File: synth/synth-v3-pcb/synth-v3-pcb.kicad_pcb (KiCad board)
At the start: 2 copper layers, 213.5 x 130 mm, 78 parts, among them J1 Keyboard, J2 15mm Touch, J3 15mm Touch, J4 3.5mm Jack, U1 LM324N, U2 LM324N, U3 LM324N, U4 Pi Pico, U5 TC1044S, U6 NJM4580D

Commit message: Released Synth V3.0
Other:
- board text added: "DO NOT PLACE COMPONENTS ON THIS SIDE OF THE BOARD"
- board text added: "LIVEWIRES SYNTH SOLDER SIDE"

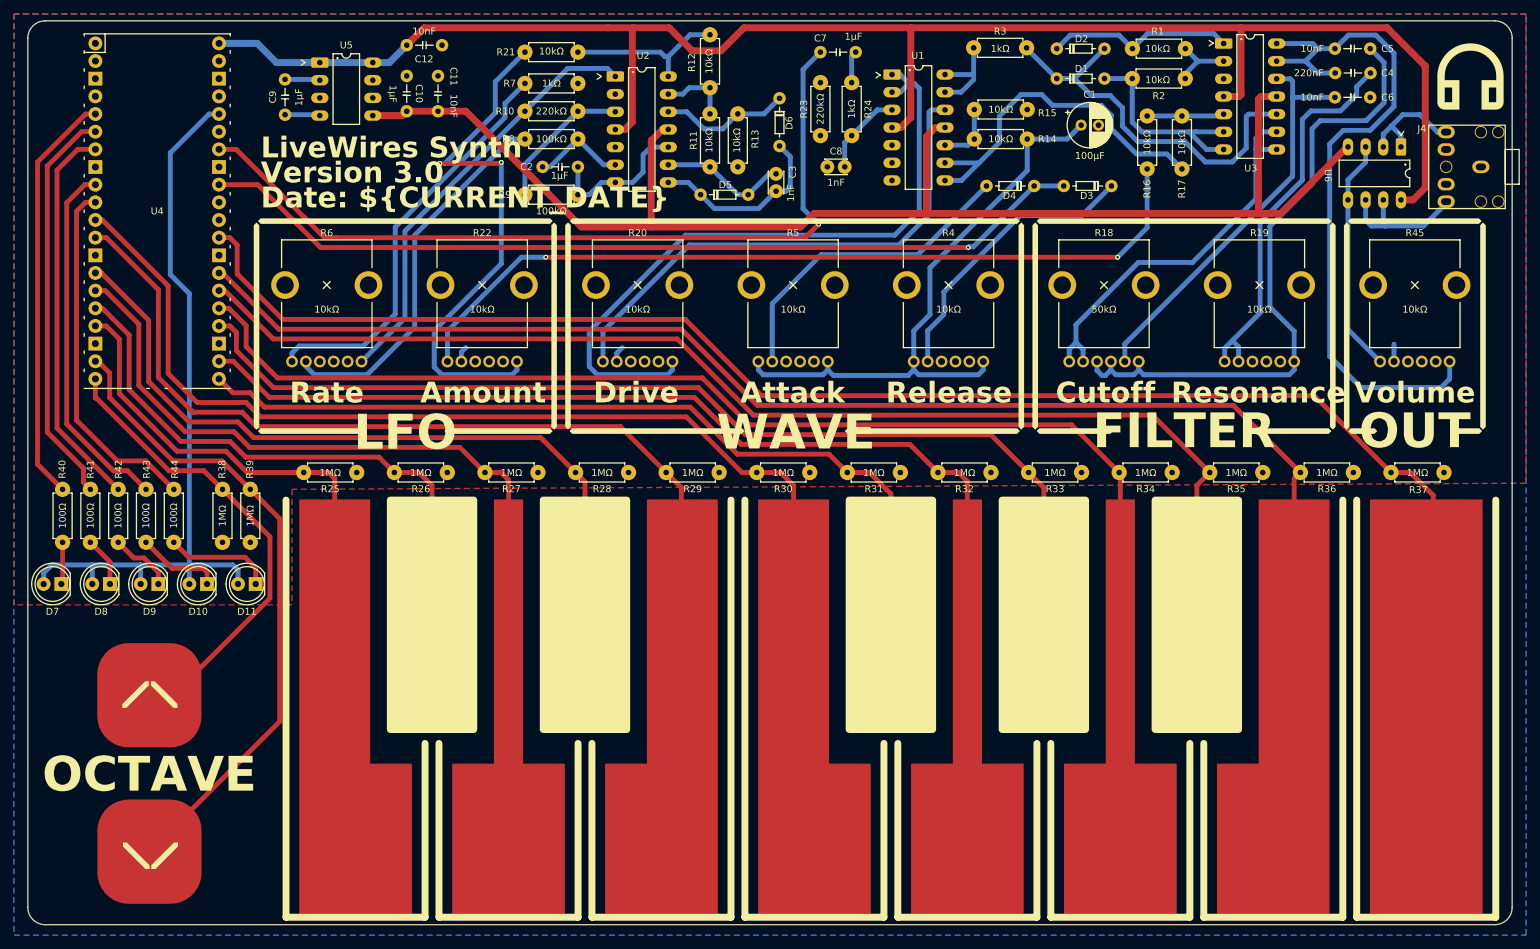
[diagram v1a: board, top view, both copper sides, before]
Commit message: Released PCB v3.1 and added knobs
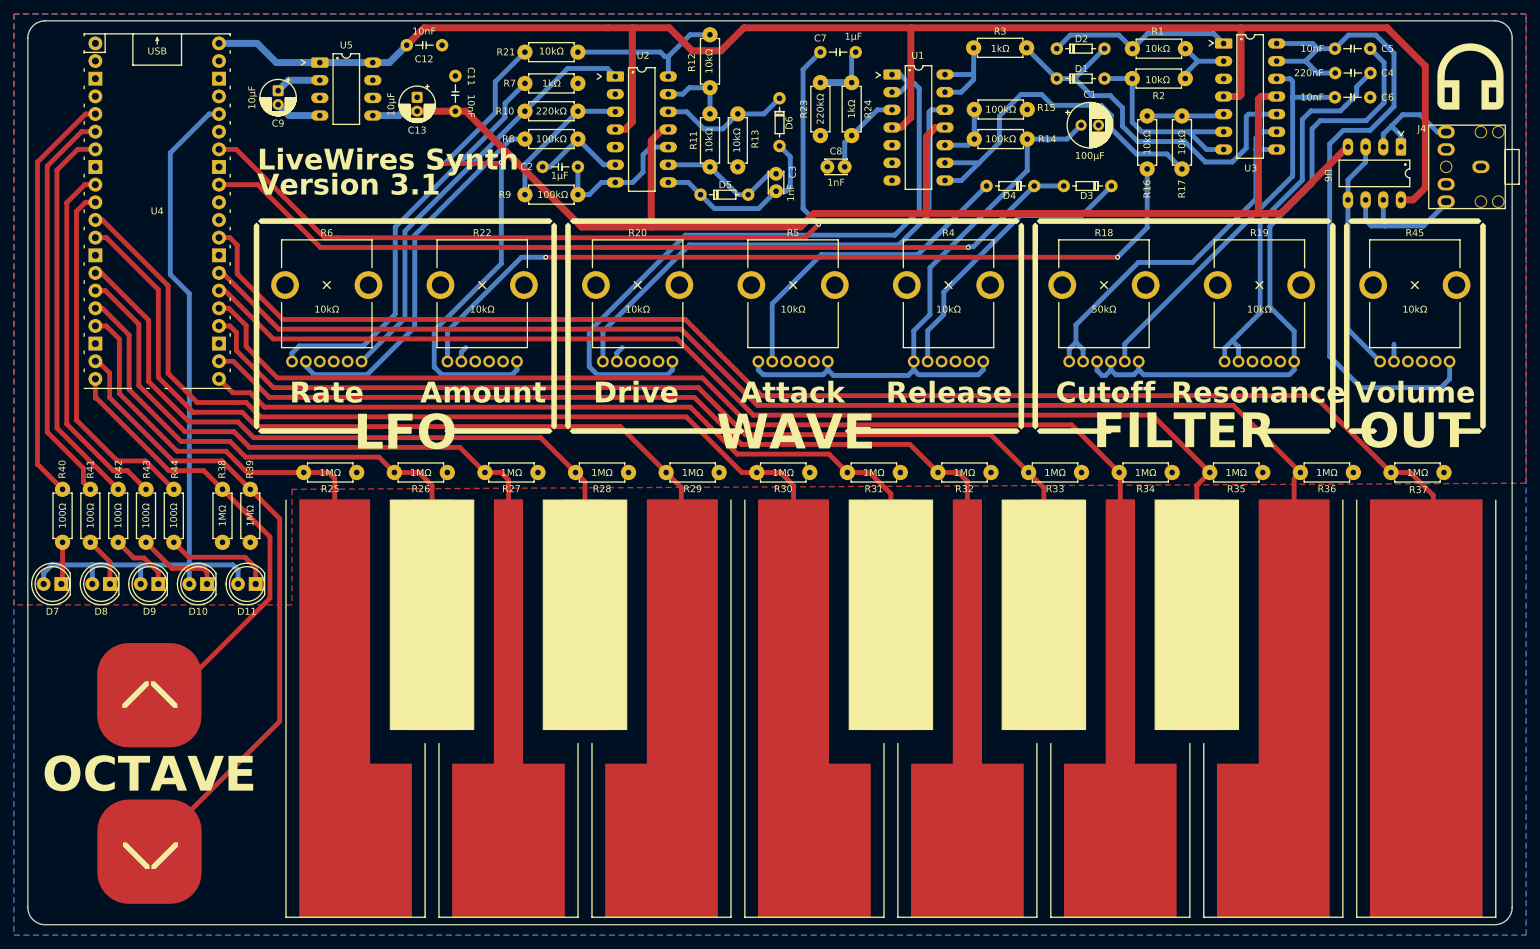
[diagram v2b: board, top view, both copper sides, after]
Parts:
- removed C10: 1µF, LiveWires:LW_CeramicCap_5.08mm
- added C13: 10µF, LiveWires:LW_CAP_Radial_D5.0mm_P2.00mm, F.Cu at (80.5, 32.0)
- C9: value 1µF -> 10µF; footprint LiveWires:LW_CeramicCap_5.08mm -> LiveWires:LW_CAP_Radial_D5.0mm_P2.00mm
- R14, R15: value 10kΩ -> 100kΩ
- moved R15 7.62 mm to (160.6, 33.7), turned to 0 degrees
- moved C11 2.50 mm to (86.0, 31.5)
- moved C9 1.36 mm to (60.5, 31.0), turned to -90 degrees
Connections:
- C9 pad 1: Net-(U5-CAP-) -> Net-(U5-CAP+)
- C9 pad 2: Net-(U5-CAP+) -> Net-(U5-CAP-)
- R15 pad 1: GND -> Net-(U1C-IN+)
- R15 pad 2: Net-(U1C-IN+) -> GND
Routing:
- net Net-(C7-Pad2): track 4.62 -> 9.12 mm
- net Net-(U5-CAP-): track 5.05 -> 6.65 mm
- net Net-(U5-CAP+): track 5.05 -> 6.62 mm
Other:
- board text added: "Version 3.1"
- board text removed: "Date: ${CURRENT_DATE}"
- board text removed: "Version 3.0"
